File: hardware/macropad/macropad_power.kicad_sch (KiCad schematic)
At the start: 20 parts, among them Q1 Q_PMOS, Q2 FS8205A, U1 TP4056-42-ESOP8, U2 DW01A, U3 RT8010AGQW

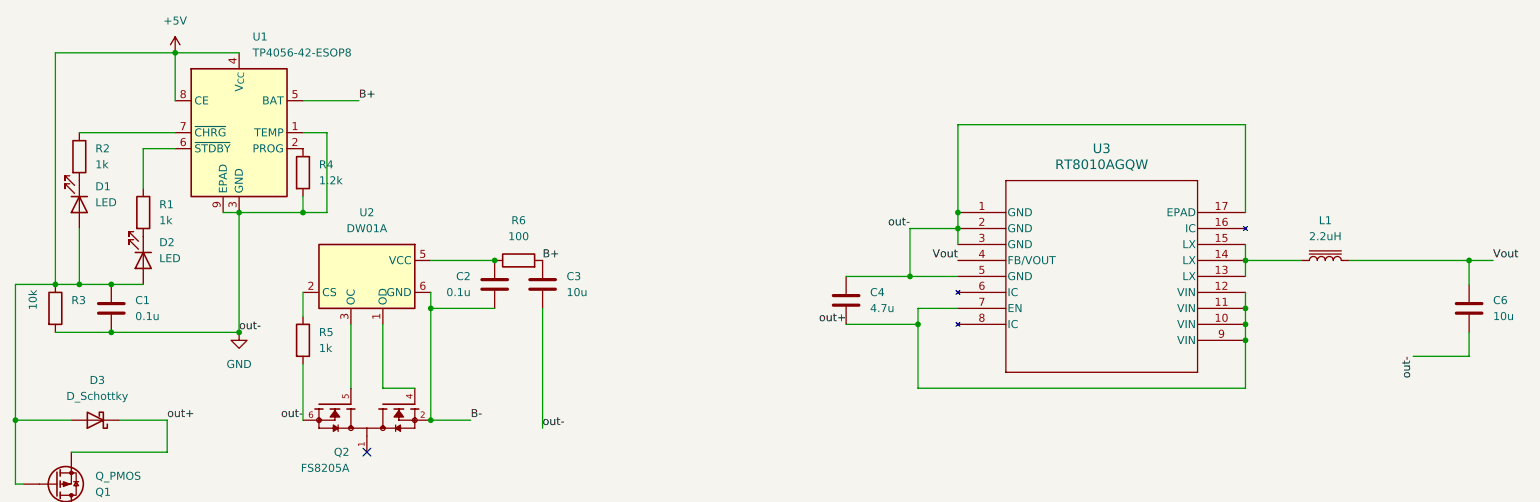
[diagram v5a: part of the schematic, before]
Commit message: changed load capacitance, added oscillator for pad
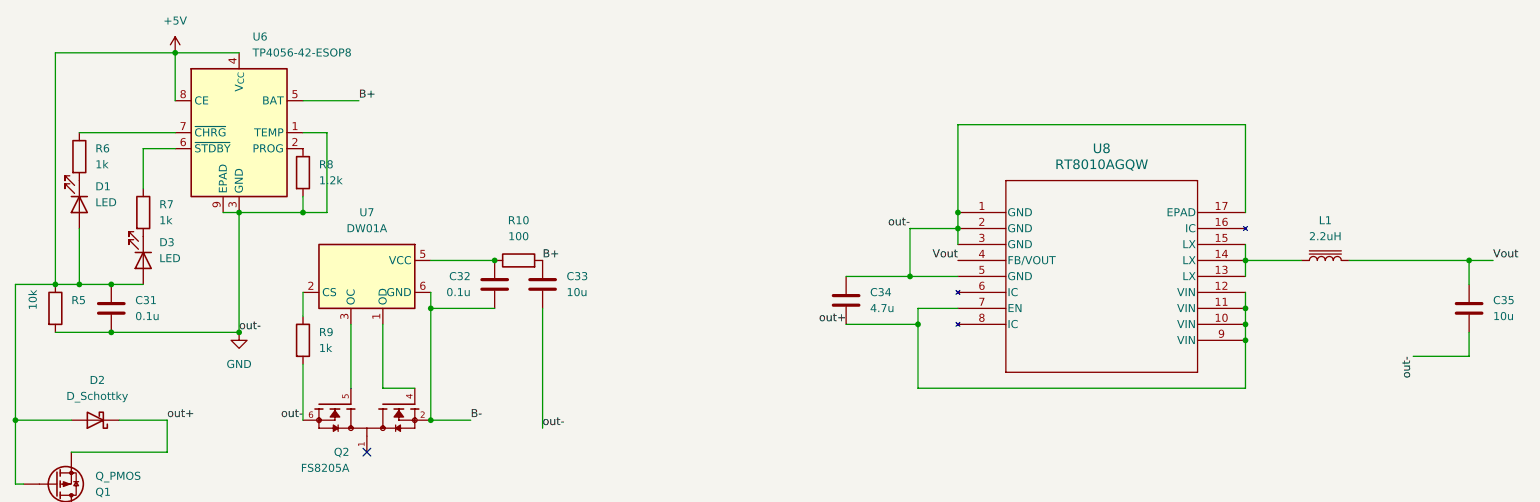
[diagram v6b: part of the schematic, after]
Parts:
- renumbered C1 to C31, C2 to C32, C3 to C33, C4 to C34, C6 to C35, D3 to D2, D2 to D3, R6 to R10, R3 to R5, R2 to R6, R1 to R7, R4 to R8, R5 to R9, U1 to U6, U2 to U7, U3 to U8
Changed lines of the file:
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@@
 		(dnp no)
 		(fields_autoplaced yes)
-		(property "Reference" "R1"
+		(property "Reference" "R7"
 			(at 113.03 120.6499 0)
 			(effects
@@
 					(unit 1)
 				)
+				(path "/228dc472-b306-4e5f-8dc5-2bf23eb4978d/5b38d27c-d7f4-4a8d-8a5e-966bba03fead"
+					(reference "R7")
+					(unit 1)
+				)
 			)
 		)
@@
 		(dnp no)
 		(fields_autoplaced yes)
-		(property "Reference" "#PWR02"
+		(property "Reference" "#PWR060"
 			(at 125.73 147.32 0)
 			(effects
@@
 					(unit 1)
 				)
+				(path "/228dc472-b306-4e5f-8dc5-2bf23eb4978d/5b38d27c-d7f4-4a8d-8a5e-966bba03fead"
+					(reference "#PWR060")
+					(unit 1)
+				)
 			)
 		)
@@
 					(unit 1)
 				)
+				(path "/228dc472-b306-4e5f-8dc5-2bf23eb4978d/5b38d27c-d7f4-4a8d-8a5e-966bba03fead"
+					(reference "D1")
+					(unit 1)
+				)
 			)
 		)
@@
 		(dnp no)
 		(fields_autoplaced yes)
-		(property "Reference" "R5"
+		(property "Reference" "R9"
 			(at 138.43 140.9699 0)
 			(effects
@@
 					(unit 1)
 				)
+				(path "/228dc472-b306-4e5f-8dc5-2bf23eb4978d/5b38d27c-d7f4-4a8d-8a5e-966bba03fead"
+					(reference "R9")
+					(unit 1)
+				)
 			)
 		)
@@
 					(unit 1)
 				)
+				(path "/228dc472-b306-4e5f-8dc5-2bf23eb4978d/5b38d27c-d7f4-4a8d-8a5e-966bba03fead"
+					(reference "L1")
+					(unit 1)
+				)
 			)
 		)
@@
 		(dnp no)
 		(fields_autoplaced yes)
-		(property "Reference" "R4"
+		(property "Reference" "R8"
 			(at 138.43 114.2999 0)
 			(effects
@@
 				(path "/228dc472-b306-4e5f-8dc5-2bf23eb4978d"
 					(reference "R4")
+					(unit 1)
+				)
+				(path "/228dc472-b306-4e5f-8dc5-2bf23eb4978d/5b38d27c-d7f4-4a8d-8a5e-966bba03fead"
+					(reference "R8")
 					(unit 1)
 				)
@@
 					(unit 1)
 				)
+				(path "/228dc472-b306-4e5f-8dc5-2bf23eb4978d/5b38d27c-d7f4-4a8d-8a5e-966bba03fead"
+					(reference "Q1")
+					(unit 1)
+				)
 			)
 		)
@@
 		(dnp no)
 		(fields_autoplaced yes)
-		(property "Reference" "R6"
+		(property "Reference" "R10"
 			(at 170.18 123.19 90)
 			(effects
@@
 					(unit 1)
 				)
+				(path "/228dc472-b306-4e5f-8dc5-2bf23eb4978d/5b38d27c-d7f4-4a8d-8a5e-966bba03fead"
+					(reference "R10")
+					(unit 1)
+				)
 			)
 		)
@@
 		(on_board yes)
 		(dnp no)
-		(property "Reference" "R3"
+		(property "Reference" "R5"
 			(at 99.06 135.8899 0)
 			(effects
@@
 					(unit 1)
 				)
+				(path "/228dc472-b306-4e5f-8dc5-2bf23eb4978d/5b38d27c-d7f4-4a8d-8a5e-966bba03fead"
+					(reference "R5")
+					(unit 1)
+				)
 			)
 		)
@@
 		(dnp no)
 		(fields_autoplaced yes)
-		(property "Reference" "D2"
+		(property "Reference" "D3"
 			(at 113.03 126.6824 90)
 			(effects
@@
 					(unit 1)
 				)
+				(path "/228dc472-b306-4e5f-8dc5-2bf23eb4978d/5b38d27c-d7f4-4a8d-8a5e-966bba03fead"
+					(reference "D3")
+					(unit 1)
+				)
 			)
 		)
@@
 		(dnp no)
 		(fields_autoplaced yes)
-		(property "Reference" "D3"
+		(property "Reference" "D2"
 			(at 103.1875 148.59 0)
 			(effects
@@
 					(unit 1)
 				)
+				(path "/228dc472-b306-4e5f-8dc5-2bf23eb4978d/5b38d27c-d7f4-4a8d-8a5e-966bba03fead"
+					(reference "D2")
+					(unit 1)
+				)
 			)
 		)
@@
 		(dnp no)
 		(fields_autoplaced yes)
-		(property "Reference" "R2"
+		(property "Reference" "R6"
 			(at 102.87 111.7599 0)
 			(effects
@@
 				(path "/228dc472-b306-4e5f-8dc5-2bf23eb4978d"
 					(reference "R2")
+					(unit 1)
+				)
+				(path "/228dc472-b306-4e5f-8dc5-2bf23eb4978d/5b38d27c-d7f4-4a8d-8a5e-966bba03fead"
+					(reference "R6")
 					(unit 1)
 				)
@@
 		(dnp no)
 		(fields_autoplaced yes)
-		(property "Reference" "C2"
+		(property "Reference" "C32"
 			(at 162.56 132.0799 0)
 			(effects
@@
 				(path "/228dc472-b306-4e5f-8dc5-2bf23eb4978d"
 					(reference "C2")
+					(unit 1)
+				)
+				(path "/228dc472-b306-4e5f-8dc5-2bf23eb4978d/5b38d27c-d7f4-4a8d-8a5e-966bba03fead"
+					(reference "C32")
 					(unit 1)
 				)
@@
 					(unit 1)
 				)
+				(path "/228dc472-b306-4e5f-8dc5-2bf23eb4978d/5b38d27c-d7f4-4a8d-8a5e-966bba03fead"
+					(reference "Q2")
+					(unit 1)
+				)
 			)
 		)
@@
 		(dnp no)
 		(fields_autoplaced yes)
-		(property "Reference" "C3"
+		(property "Reference" "C33"
 			(at 177.8 132.0799 0)
 			(effects
@@
 					(unit 1)
 				)
+				(path "/228dc472-b306-4e5f-8dc5-2bf23eb4978d/5b38d27c-d7f4-4a8d-8a5e-966bba03fead"
+					(reference "C33")
+					(unit 1)
+				)
 			)
 		)
@@
 		(dnp no)
 		(fields_autoplaced yes)
-		(property "Reference" "#PWR01"
+		(property "Reference" "#PWR059"
 			(at 115.57 100.33 0)
 			(effects
@@
 				(path "/228dc472-b306-4e5f-8dc5-2bf23eb4978d"
 					(reference "#PWR01")
+					(unit 1)
+				)
+				(path "/228dc472-b306-4e5f-8dc5-2bf23eb4978d/5b38d27c-d7f4-4a8d-8a5e-966bba03fead"
+					(reference "#PWR059")
 					(unit 1)
 				)
@@
 		(dnp no)
 		(fields_autoplaced yes)
-		(property "Reference" "U2"
+		(property "Reference" "U7"
 			(at 146.05 121.92 0)
 			(effects
@@
 					(unit 1)
 				)
+				(path "/228dc472-b306-4e5f-8dc5-2bf23eb4978d/5b38d27c-d7f4-4a8d-8a5e-966bba03fead"
+					(reference "U7")
+					(unit 1)
+				)
 			)
 		)
@@
 		(dnp no)
 		(fields_autoplaced yes)
-		(property "Reference" "C4"
+		(property "Reference" "C34"
 			(at 226.06 134.6199 0)
 			(effects
@@
 					(unit 1)
 				)
+				(path "/228dc472-b306-4e5f-8dc5-2bf23eb4978d/5b38d27c-d7f4-4a8d-8a5e-966bba03fead"
+					(reference "C34")
+					(unit 1)
+				)
 			)
 		)
@@
 		(dnp no)
 		(fields_autoplaced yes)
-		(property "Reference" "U3"
+		(property "Reference" "U8"
 			(at 262.89 111.76 0)
 			(effects
@@
 					(unit 1)
 				)
+				(path "/228dc472-b306-4e5f-8dc5-2bf23eb4978d/5b38d27c-d7f4-4a8d-8a5e-966bba03fead"
+					(reference "U8")
+					(unit 1)
+				)
 			)
 		)
@@
 		(dnp no)
 		(fields_autoplaced yes)
-		(property "Reference" "U1"
+		(property "Reference" "U6"
 			(at 127.8733 93.98 0)
 			(effects
@@
 					(unit 1)
 				)
+				(path "/228dc472-b306-4e5f-8dc5-2bf23eb4978d/5b38d27c-d7f4-4a8d-8a5e-966bba03fead"
+					(reference "U6")
+					(unit 1)
+				)
 			)
 		)
@@
 		(dnp no)
 		(fields_autoplaced yes)
-		(property "Reference" "C1"
+		(property "Reference" "C31"
 			(at 109.22 135.8899 0)
 			(effects
@@
 					(unit 1)
 				)
+				(path "/228dc472-b306-4e5f-8dc5-2bf23eb4978d/5b38d27c-d7f4-4a8d-8a5e-966bba03fead"
+					(reference "C31")
+					(unit 1)
+				)
 			)
 		)
@@
 		(dnp no)
 		(fields_autoplaced yes)
-		(property "Reference" "C6"
+		(property "Reference" "C35"
 			(at 325.12 135.8899 0)
 			(effects
@@
 					(unit 1)
 				)
+				(path "/228dc472-b306-4e5f-8dc5-2bf23eb4978d/5b38d27c-d7f4-4a8d-8a5e-966bba03fead"
+					(reference "C35")
+					(unit 1)
+				)

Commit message: updated footprints
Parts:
- C31, C32, C34: footprint (none) -> Capacitor_SMD:C_0603_1608Metric
- C33, C35: footprint (none) -> Capacitor_SMD:C_0805_2012Metric
- D1, D3: footprint (none) -> LED_SMD:LED_0805_2012Metric
- Q1: footprint (none) -> Package_TO_SOT_SMD:SOT-23-3
- Q2: footprint FS8205A:SOP65P640X120-8N -> (none)
- R10, R6, R7, R8, R9: footprint (none) -> Resistor_SMD:R_0603_1608Metric
- R5: footprint (none) -> Resistor_SMD:R_0402_1005Metric
- U8: footprint WQFN16_RT8010_RIT -> (none)
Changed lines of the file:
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@@
 			)
 		)
-		(property "Footprint" ""
+		(property "Footprint" "Resistor_SMD:R_0603_1608Metric"
 			(at 108.712 121.92 90)
 			(effects
@@
 			)
 		)
-		(property "Footprint" ""
+		(property "Footprint" "LED_SMD:LED_0805_2012Metric"
 			(at 100.33 120.65 0)
 			(effects
@@
 			)
 		)
-		(property "Footprint" ""
+		(property "Footprint" "Resistor_SMD:R_0603_1608Metric"
 			(at 134.112 142.24 90)
 			(effects
@@
 			)
 		)
-		(property "Footprint" ""
+		(property "Footprint" "Resistor_SMD:R_0603_1608Metric"
 			(at 134.112 115.57 90)
 			(effects
@@
 			)
 		)
-		(property "Footprint" ""
+		(property "Footprint" "Package_TO_SOT_SMD:SOT-23-3"
 			(at 101.6 167.64 0)
 			(effects
@@
 			)
 		)
-		(property "Footprint" ""
+		(property "Footprint" "Resistor_SMD:R_0603_1608Metric"
 			(at 170.18 131.318 90)
 			(effects
@@
 			)
 		)
-		(property "Footprint" ""
+		(property "Footprint" "Resistor_SMD:R_0402_1005Metric"
 			(at 94.742 137.16 90)
 			(effects
@@
 			)
 		)
-		(property "Footprint" ""
+		(property "Footprint" "LED_SMD:LED_0805_2012Metric"
 			(at 110.49 129.54 0)
 			(effects
@@
 			)
 		)
-		(property "Footprint" ""
+		(property "Footprint" "Resistor_SMD:R_0603_1608Metric"
 			(at 98.552 113.03 90)
 			(effects
@@
 			)
 		)
-		(property "Footprint" ""
+		(property "Footprint" "Capacitor_SMD:C_0603_1608Metric"
 			(at 165.4048 137.16 0)
 			(effects
@@
 			)
 		)
-		(property "Footprint" "FS8205A:SOP65P640X120-8N"
+		(property "Footprint" ""
 			(at 146.05 154.94 0)
 			(effects
@@
 			)
 		)
-		(property "Footprint" ""
+		(property "Footprint" "Capacitor_SMD:C_0805_2012Metric"
 			(at 174.9552 137.16 0)
 			(effects
@@
 			)
 		)
-		(property "Footprint" ""
+		(property "Footprint" "Capacitor_SMD:C_0603_1608Metric"
 			(at 223.2152 139.7 0)
 			(effects
@@
 			)
 		)
-		(property "Footprint" "WQFN16_RT8010_RIT"
+		(property "Footprint" ""
 			(at 240.03 121.92 0)
 			(effects
@@
 			)
 		)
-		(property "Footprint" ""
+		(property "Footprint" "Capacitor_SMD:C_0603_1608Metric"
 			(at 106.3752 140.97 0)
 			(effects
@@
 			)
 		)
-		(property "Footprint" ""
+		(property "Footprint" "Capacitor_SMD:C_0805_2012Metric"
 			(at 322.2752 140.97 0)
 			(effects

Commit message: updated footprints
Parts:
- L1: footprint (none) -> Inductor_SMD:L_10.4x10.4_H4.8
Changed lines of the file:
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@@
 			)
 		)
-		(property "Footprint" ""
+		(property "Footprint" "Inductor_SMD:L_10.4x10.4_H4.8"
 			(at 298.45 129.54 0)
 			(effects
